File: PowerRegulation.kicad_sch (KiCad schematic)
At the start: 29 parts, among them J5 XT60-M, K1 PR30-24V-450-1A, Q7 BSS138, U6 TPS5430DDA, U7 TPS5430DDA, U8 XC6206P332MR

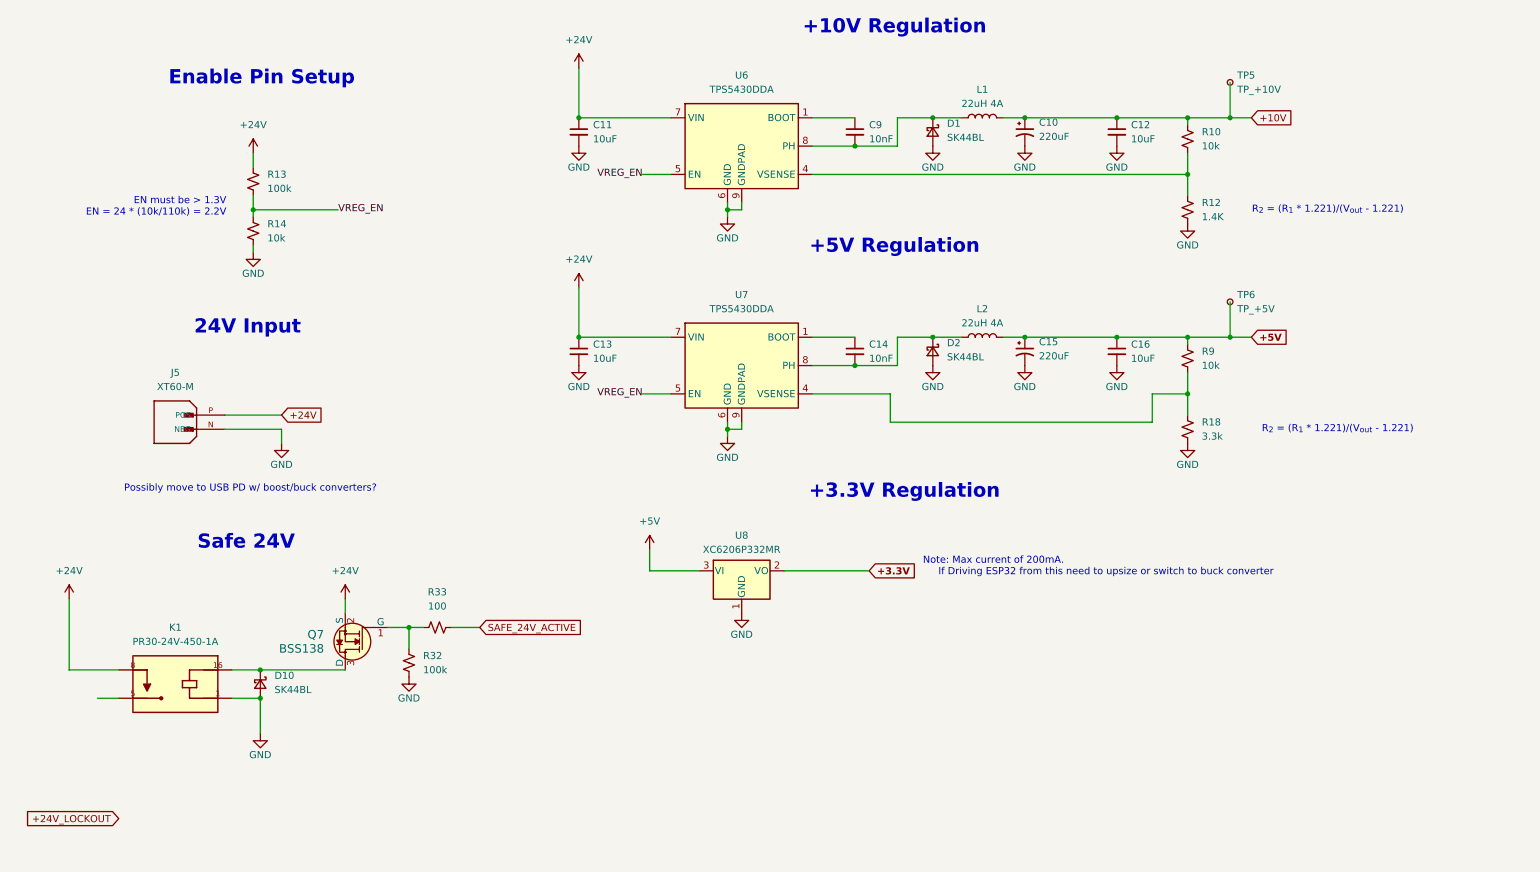
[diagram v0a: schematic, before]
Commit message: Add load cell inputs
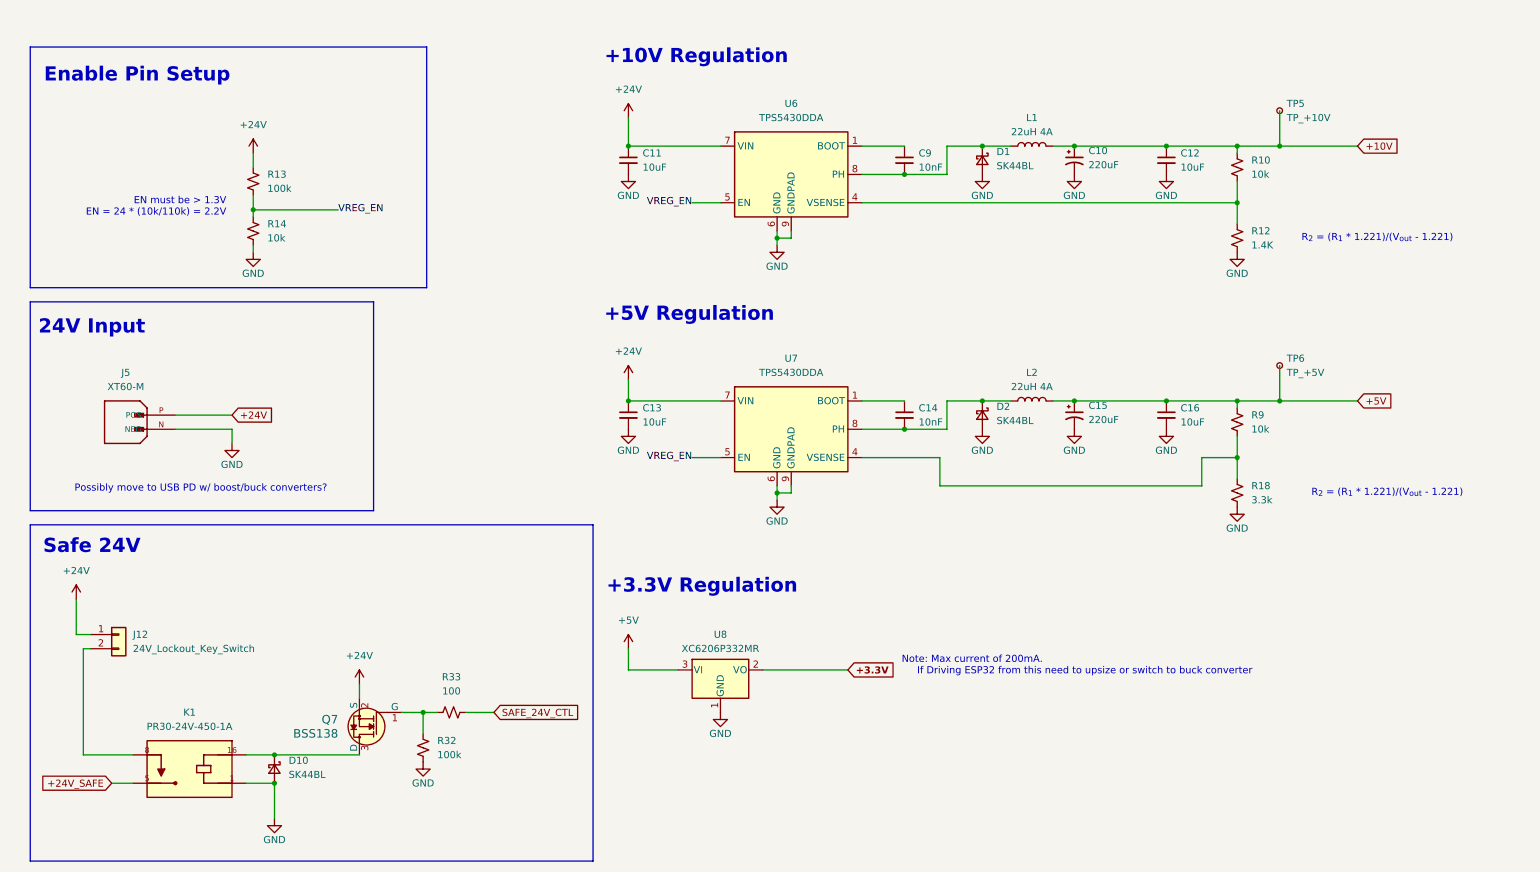
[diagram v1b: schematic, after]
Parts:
- added J12: 24V_Lockout_Key_Switch, Connector_JST:JST_XH_B2B-XH-A_1x02_P2.50mm_Vertical, symbol Connector_Generic:Conn_01x02
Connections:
- net +24V: now also J12.1 (Pin_1); no longer K1.8
- net +24V_SAFE: now reaches K1.5
- net SAFE_24V_ACTIVE renamed SAFE_24V_CTL
- new net: J12.2 (Pin_2), K1.8
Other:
- moved on the sheet: C10, C11, C12, C13, C14, C15, C16, C9, D1, D10, D2, J5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

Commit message: v0.1 sch. Add devkit c1 footprint
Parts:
- C14: footprint (none) -> Capacitor_SMD:C_0402_1005Metric
- D1, D2: footprint (none) -> Diode_SMD:D_SMB
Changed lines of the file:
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@@
 			)
 		)
-		(property "Footprint" ""
+		(property "Footprint" "Diode_SMD:D_SMB"
 			(at 194.31 87.63 90)
 			(effects
@@
 			)
 		)
-		(property "Footprint" ""
+		(property "Footprint" "Capacitor_SMD:C_0402_1005Metric"
 			(at 180.34 87.63 0)
 			(effects
@@
 			)
 		)
-		(property "Footprint" ""
+		(property "Footprint" "Diode_SMD:D_SMB"
 			(at 194.31 41.91 90)
 			(effects

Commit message: Add all footprints
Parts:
- removed K1: PR30-24V-450-1A, Solenoid Safeguard:RELAY_PR30-24V-450-1A, symbol PR30-24V-450-1A:PR30-24V-450-1A
- added K4: G5LE-1, Relay_THT:Relay_SPDT_Omron-G5LE-1, symbol Relay:G5LE-1
- J5: footprint XT60-M:AMASS_XT60-M -> Connector_AMASS:AMASS_XT60PW-F_1x02_P7.20mm_Horizontal
- R32: value 100k -> 10k; LCSC C25530 -> C25531; MPN 0402WGJ0104TCE -> 0402WGJ0103TCE
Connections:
- net +24V_SAFE: now also K4.3
- net GND: now also K4.5
- net at D10.1 (K), Q7.3 (D): now also K4.2
- net at J12.2 (Pin_2): now also K4.1
- no-connect marks 0 -> 2
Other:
- moved on the sheet: D10, Q7, R33

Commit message: Almost done routing
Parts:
- removed R14: 10k, Resistor_SMD:R_0201_0603Metric, symbol Device:R_Small_US
- added R39: 10k, Resistor_SMD:R_0402_1005Metric, symbol Device:R_Small_US
- TP5, TP6: footprint TestPoint:TestPoint_Pad_D2.0mm -> TestPoint:TestPoint_Pad_D1.0mm
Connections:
- net GND: now also R39.2
- net VREG_EN: now also R39.1
- net +10V_SENSE: now reaches R10.2, R12.1, U6.4 (VSENSE)
- net LOCKOUT_RLY_CTRL_FET: now reaches Q7.1 (G), R32.1, R33.1
- net LOCKOUT_RLY_+VE: now reaches D10.1 (K), K4.2, Q7.3 (D)
- net +10V_REG_BOOT: now reaches C9.1, U6.1 (BOOT)
- net +10V_REG_PH: now reaches C9.2, D1.1 (K), L1.1, U6.8 (PH)
- net +24V_POST_LOCKOUT: now reaches J12.2 (Pin_2), K4.1
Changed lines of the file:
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@@
 	(wire
 		(pts
-			(xy 104.14 134.62) (xy 109.22 134.62)
+			(xy 104.14 134.62) (xy 113.03 134.62)
 		)
 		(stroke
@@
 		)
 	)
+	(label "+24V_POST_LOCKOUT"
+		(at 31.75 142.24 0)
+		(effects
+			(font
+				(size 1.27 1.27)
+			)
+			(justify left bottom)
+		)
+	)
+	(label "+10V_OUT"
+		(at 223.52 39.37 90)
+		(effects
+			(font
+				(size 1.27 1.27)
+			)
+			(justify left bottom)
+		)
+	)
+	(label "+10V_REG_BOOT"
+		(at 175.26 39.37 90)
+		(effects
+			(font
+				(size 1.27 1.27)
+			)
+			(justify left bottom)
+		)
+	)
+	(label "LOCKOUT_RLY_CTRL_FET"
+		(at 95.25 134.62 90)
+		(effects
+			(font
+				(size 1.27 1.27)
+			)
+			(justify left bottom)
+		)
+	)
+	(label "+10V_SENSE"
+		(at 180.34 49.53 270)
+		(effects
+			(font
+				(size 1.27 1.27)
+			)
+			(justify right bottom)
+		)
+	)
+	(label "LOCKOUT_RLY_CTRL_MCU"
+		(at 109.22 134.62 90)
+		(effects
+			(font
+				(size 1.27 1.27)
+			)
+			(justify left bottom)
+		)
+	)
+	(label "+24V_PRE_LOCKOUT"
+		(at 31.75 123.19 0)
+		(effects
+			(font
+				(size 1.27 1.27)
+			)
+			(justify left bottom)
+		)
+	)
+	(label "LOCKOUT_RLY_+VE"
+		(at 58.42 142.24 0)
+		(effects
+			(font
+				(size 1.27 1.27)
+			)
+			(justify left bottom)
+		)
+	)
+	(label "+10V_REG_PH"
+		(at 189.23 39.37 90)
+		(effects
+			(font
+				(size 1.27 1.27)
+			)
+			(justify left bottom)
+		)
+	)
 	(label "VREG_EN"
 		(at 142.24 95.25 180)
@@
 	(global_label "SAFE_24V_CTL"
 		(shape input)
-		(at 109.22 134.62 0)
+		(at 113.03 134.62 0)
 		(fields_autoplaced yes)
 		(effects
@@
 		)
 		(property "Intersheetrefs" "${INTERSHEET_REFS}"
-			(at 125.4494 134.62 0)
+			(at 129.2594 134.62 0)
 			(effects
 				(font
@@
 			)
 		)
-		(property "Footprint" "TestPoint:TestPoint_Pad_D2.0mm"
+		(property "Footprint" "TestPoint:TestPoint_Pad_D1.0mm"
 			(at 252.73 78.74 0)
 			(effects
@@
 			)
 		)
-		(property "Footprint" "TestPoint:TestPoint_Pad_D2.0mm"
+		(property "Footprint" "TestPoint:TestPoint_Pad_D1.0mm"
 			(at 252.73 33.02 0)
 			(effects
@@
 	)
 	(symbol
-		(lib_id "Device:R_Small_US")
-		(at 63.5 54.61 0)
-		(unit 1)
-		(exclude_from_sim no)
-		(in_bom yes)
-		(on_board yes)
-		(dnp no)
-		(fields_autoplaced yes)
-		(property "Reference" "R14"
-			(at 66.04 53.3399 0)
-			(effects
-				(font
-					(size 1.27 1.27)
-				)
-				(justify left)
-			)
-		)
-		(property "Value" "10k"
-			(at 66.04 55.8799 0)
-			(effects
-				(font
-					(size 1.27 1.27)
-				)
-				(justify left)
-			)
-		)
-		(property "Footprint" "Resistor_SMD:R_0201_0603Metric"
-			(at 63.5 54.61 0)
-			(effects
-				(font
-					(size 1.27 1.27)
-				)
-				(hide yes)
-			)
-		)
-		(property "Datasheet" "~"
-			(at 63.5 54.61 0)
-			(effects
-				(font
-					(size 1.27 1.27)
-				)
-				(hide yes)
-			)
-		)
-		(property "Description" "Resistor, small US symbol"
-			(at 63.5 54.61 0)
-			(effects
-				(font
-					(size 1.27 1.27)
-				)
-				(hide yes)
-			)
-		)
-		(property "MPN" "0603WAJ0103T5E"
-			(at 63.5 54.61 0)
-			(effects
-				(font
-					(size 1.27 1.27)
-				)
-				(hide yes)
-			)
-		)
-		(property "LCSC" "C15401"
-			(at 63.5 54.61 0)
-			(effects
-				(font
-					(size 1.27 1.27)
-				)
-				(hide yes)
-			)
-		)
-		(pin "2"
-		)
-		(pin "1"
-		)
-		(instances
-			(project "nexus"
-				(path "/226c5870-4123-4efa-a2b3-b42d02f59bb7/9fa93f08-739d-4753-8e9a-eafbcf15bffc"
-					(reference "R14")
-					(unit 1)
-				)
-			)
-		)
-	)
-	(symbol
 		(lib_id "power:+24V")
 		(at 130.81 81.28 0)
@@
 					(unit 1)
 				)
+			)
+		)
+	)
+	(symbol
+		(lib_id "Device:R_Small_US")
+		(at 63.5 54.61 0)
+		(unit 1)
+		(exclude_from_sim no)
+		(in_bom yes)
+		(on_board yes)
+		(dnp no)
+		(fields_autoplaced yes)
+		(property "Reference" "R39"
+			(at 66.04 53.3399 0)
+			(effects
+				(font
+					(size 1.27 1.27)
+				)
+				(justify left)
+			)
+		)
+		(property "Value" "10k"
+			(at 66.04 55.8799 0)
+			(effects
+				(font
+					(size 1.27 1.27)
+				)
+				(justify left)
+			)
+		)
+		(property "Footprint" "Resistor_SMD:R_0402_1005Metric"
+			(at 63.5 54.61 0)
+			(effects
+				(font
+					(size 1.27 1.27)
+				)
+				(hide yes)
+			)
+		)
+		(property "Datasheet" "~"
+			(at 63.5 54.61 0)
+			(effects
+				(font
+					(size 1.27 1.27)
+				)
+				(hide yes)
+			)
+		)
+		(property "Description" "Resistor, small US symbol"
+			(at 63.5 54.61 0)
+			(effects
+				(font
+					(size 1.27 1.27)
+				)
+				(hide yes)
+			)
+		)
+		(property "LCSC" "C25531"
+			(at 63.5 54.61 0)
+			(effects
+				(font
+					(size 1.27 1.27)
+				)
+				(hide yes)
+			)
+		)
+		(property "MPN" "0402WGJ0103TCE"
+			(at 63.5 54.61 0)
+			(effects
+				(font
+					(size 1.27 1.27)
+				)
+				(hide yes)
+			)
+		)
+		(pin "2"
+		)
+		(pin "1"
+		)
+		(instances
+			(project "nexus"
+				(path "/226c5870-4123-4efa-a2b3-b42d02f59bb7/9fa93f08-739d-4753-8e9a-eafbcf15bffc"
+					(reference "R39")
+					(unit 1)
+				)

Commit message: Fix J5
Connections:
- net +24V: now also J5.1 (POS); no longer J5.P (POS)
- net GND: now also J5.2 (NEG); no longer J5.N (NEG)
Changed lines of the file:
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@@
 			)
 		)
-		(pin "P"
+		(pin "2"
 		)
-		(pin "N"
+		(pin "1"
 		)
 		(instances

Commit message: routing broken
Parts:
- renumbered C13 to C10, C9 to C11, C14 to C12, C10 to C13, C15 to C14, C12 to C15, C11 to C9, D10 to D7, D1 to D8, D2 to D9, J12 to J11, J5 to J12, K4 to K1, R13 to R23, R39 to R24, R32 to R25, R33 to R26, R10 to R27, R12 to R28, R9 to R29, R18 to R30, U8 to U6, U6 to U7, U7 to U8

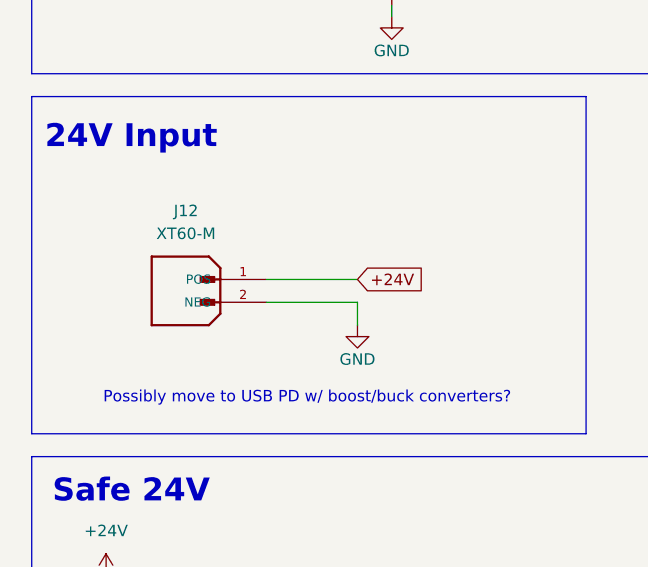
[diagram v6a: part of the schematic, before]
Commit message: Fix connector references
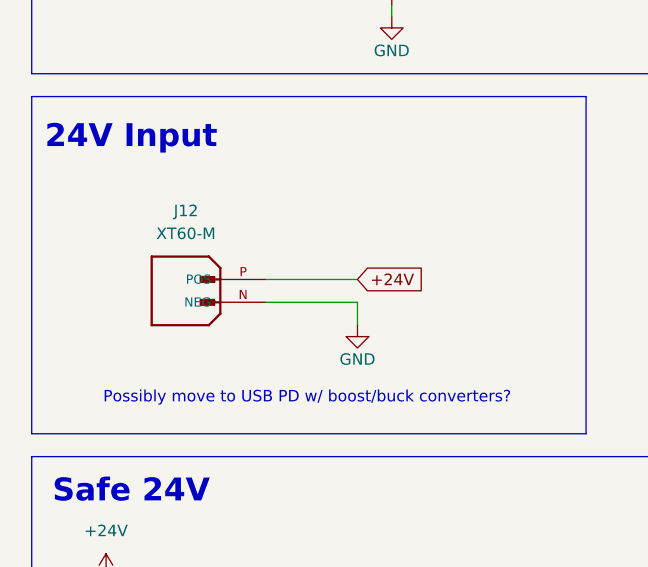
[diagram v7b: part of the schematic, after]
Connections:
- net +24V: now also J12.P (POS); no longer J12.1 (POS)
- net GND: now also J12.N (NEG); no longer J12.2 (NEG)
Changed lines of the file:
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@@
 			)
 		)
-		(pin "2"
+		(pin "N"
 		)
-		(pin "1"
+		(pin "P"
 		)
 		(instances

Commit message: Route buck converters
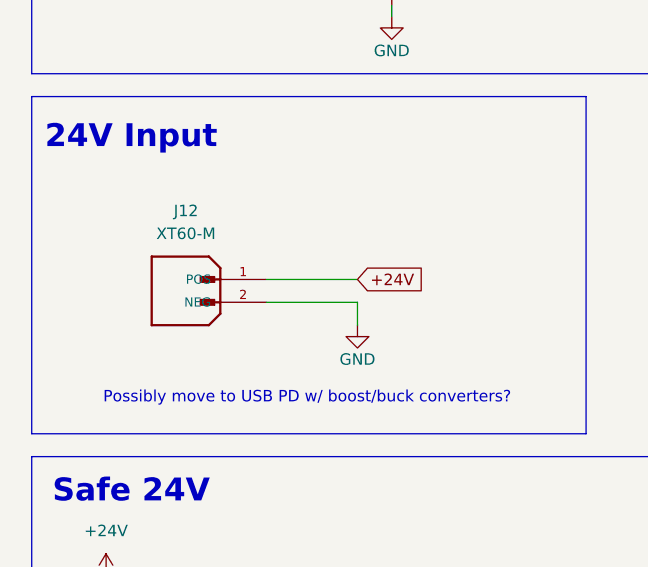
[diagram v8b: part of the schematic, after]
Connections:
- net +24V: now also J12.1 (POS); no longer J12.P (POS)
- net GND: now also J12.2 (NEG); no longer J12.N (NEG)
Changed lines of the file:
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@@
 			)
 		)
-		(pin "N"
+		(pin "2"
 		)
-		(pin "P"
+		(pin "1"
 		)
 		(instances
